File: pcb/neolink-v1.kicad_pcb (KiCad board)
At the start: 2 copper layers, 50 x 80 mm, 11 parts, among them J1 ESP32_2x16, J10 ANT_GSM, J2 SIM800L_1x6, J3 MAX31865_1, J4 MAX31865_2, J5 SHT35_1, J6 SHT35_2, J7 PT100_1, J8 PT100_2, J9 LiPo

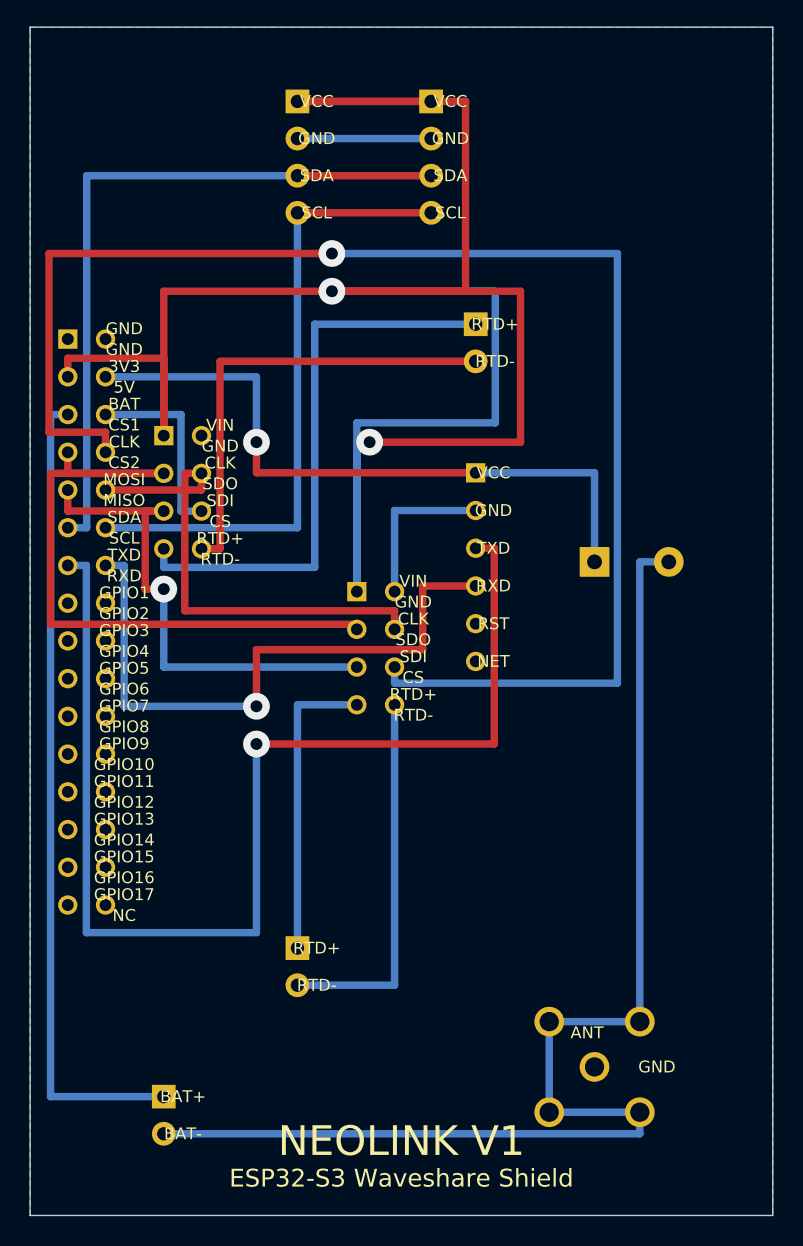
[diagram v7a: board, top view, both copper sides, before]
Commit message: fix: resolve all routing FALLBACKs with explicit pre-routes
- Add manual pre-routes for MOSI_SPI (J1→J3→J4) and TXD_SIM (J1→J2)
  to bypass the congested J1-column routing corridor
- MOSI exits left to x=6.46 (preserves x=10.16/10.42 for CS_MAX1 via
  and MISO F.Cu paths used by the algorithmic router)
- TXD_SIM exits left to board edge, crosses above J3 at y=24.81,
  arrives at J2 horizontally avoiding J3 RTD1_P at y=35.12
- Revert routing hints to original fast config (RTD1_N forced F.Cu)
- DRC result: 0 tracks_crossing, 0 shorting_items, 0 unconnected nets
- Export updated Gerbers

Co-authored-by: Cursor <cursoragent@cursor.com>
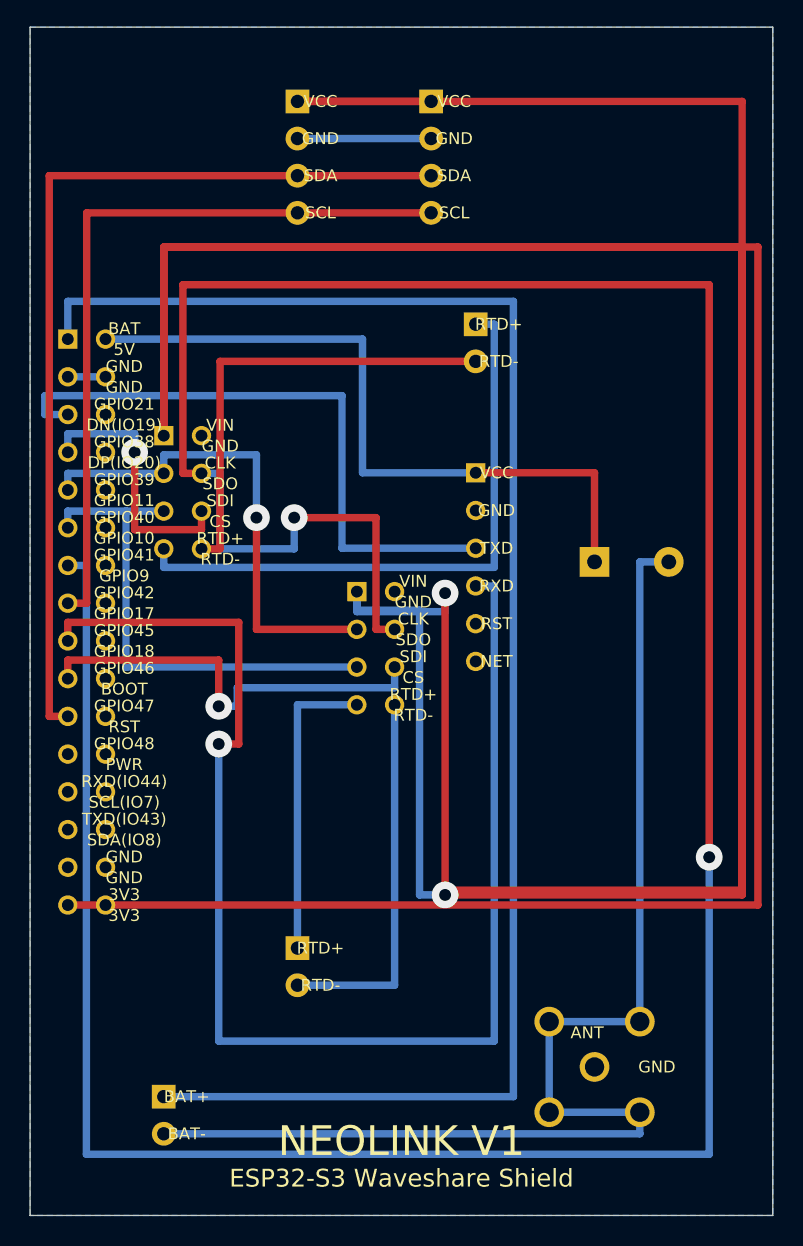
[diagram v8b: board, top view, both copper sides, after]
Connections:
- J1 pad 1: GND -> BAT
- J1 pad 10: MISO_SPI -> (no net)
- J1 pad 11: I2C_SDA -> MOSI_SPI
- J1 pad 12: I2C_SCL -> (no net)
- J1 pad 13: TXD_SIM -> MISO_SPI
- J1 pad 14: RXD_SIM -> (no net)
- J1 pad 15: GPIO1 -> I2C_SCL
- J1 pad 16: GPIO2 -> (no net)
- J1 pad 17: GPIO3 -> RXD_SIM
- J1 pad 18: GPIO4 -> (no net)
- J1 pad 19: GPIO5 -> CS_MAX2
- J1 pad 2: GND -> ~{VCC_5V}
- J1 pad 20: GPIO6 -> (no net)
- J1 pad 21: GPIO7 -> I2C_SDA
- J1 pad 22: GPIO8 -> (no net)
- J1 pad 23: GPIO9 -> (no net)
- J1 pad 24: GPIO10 -> (no net)
- J1 pad 25: GPIO11 -> (no net)
- J1 pad 26: GPIO12 -> (no net)
- J1 pad 27: GPIO13 -> (no net)
- J1 pad 28: GPIO14 -> (no net)
- J1 pad 29: GPIO15 -> GND
- J1 pad 3: ~{VCC_3V3} -> GND
- J1 pad 30: GPIO16 -> GND
- J1 pad 31: GPIO17 -> ~{VCC_3V3}
- J1 pad 32: (no net) -> ~{VCC_3V3}
- J1 pad 4: ~{VCC_5V} -> GND
- J1 pad 5: BAT -> TXD_SIM
- J1 pad 6: CS_MAX1 -> (no net)
- J1 pad 7: CLK_SPI -> CS_MAX1
- J1 pad 8: CS_MAX2 -> (no net)
- J1 pad 9: MOSI_SPI -> CLK_SPI
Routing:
- net ~{VCC_3V3}: track 160.5 -> 425.7 mm
- net MISO_SPI: track 33.3 -> 218.4 mm, vias 0 -> 2
- net CS_MAX2: track 100.5 -> 29.0 mm
- net BAT: track 54.7 -> 109.6 mm
- net RXD_SIM: track 42.5 -> 92.7 mm
- net TXD_SIM: track 80.6 -> 42.1 mm, vias 1 -> 0
- net I2C_SDA: track 48.2 -> 63.4 mm
- net CLK_SPI: track 46.6 -> 33.6 mm, vias 0 -> 1
- net GND: track 104.6 -> 96.2 mm
- net I2C_SCL: track 43.1 -> 50.7 mm
- net CS_MAX1: track 13.0 -> 18.0 mm, vias 0 -> 1
- net ~{VCC_5V}: track 45.4 -> 47.9 mm, vias 1 -> 0
- net RTD1_P: track 38.6 -> 41.1 mm
- net MOSI_SPI: track 33.9 -> 33.6 mm, vias 1 -> 0
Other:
- board text added: "BOOT"
- board text added: "DN(IO19)"
- board text added: "DP(IO20)"
- board text added: "GPIO18"
- board text added: "GPIO21"
- board text added: "GPIO38"
- board text added: "GPIO39"
- board text added: "GPIO40"
- board text added: "GPIO41"
- board text added: "GPIO42"
- board text added: "GPIO45"
- board text added: "GPIO46"
- board text added: "GPIO47"
- board text added: "GPIO48"
- board text added: "PWR"
- board text added: "RXD(IO44)"
- board text added: "SCL(IO7)"
- board text added: "SDA(IO8)"
- board text added: "TXD(IO43)"
- board text removed: "CS1"
- board text removed: "CS2"
- board text removed: "GPIO1"
- board text removed: "GPIO12"
- board text removed: "GPIO13"
- board text removed: "GPIO14"
- board text removed: "GPIO15"
- board text removed: "GPIO16"
- board text removed: "GPIO2"
- board text removed: "GPIO3"
- board text removed: "GPIO4"
- board text removed: "GPIO5"
- board text removed: "GPIO6"
- board text removed: "GPIO7"
- board text removed: "GPIO8"
- board text removed: "MISO"
- board text removed: "MOSI"
- board text removed: "NC"
